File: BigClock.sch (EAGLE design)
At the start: 50 parts, among them IC12 LM317MBT, IC16 7805, IC5 74LS47N, IC6 74LS47N, IC7 74LS47N, IC8 74LS47N

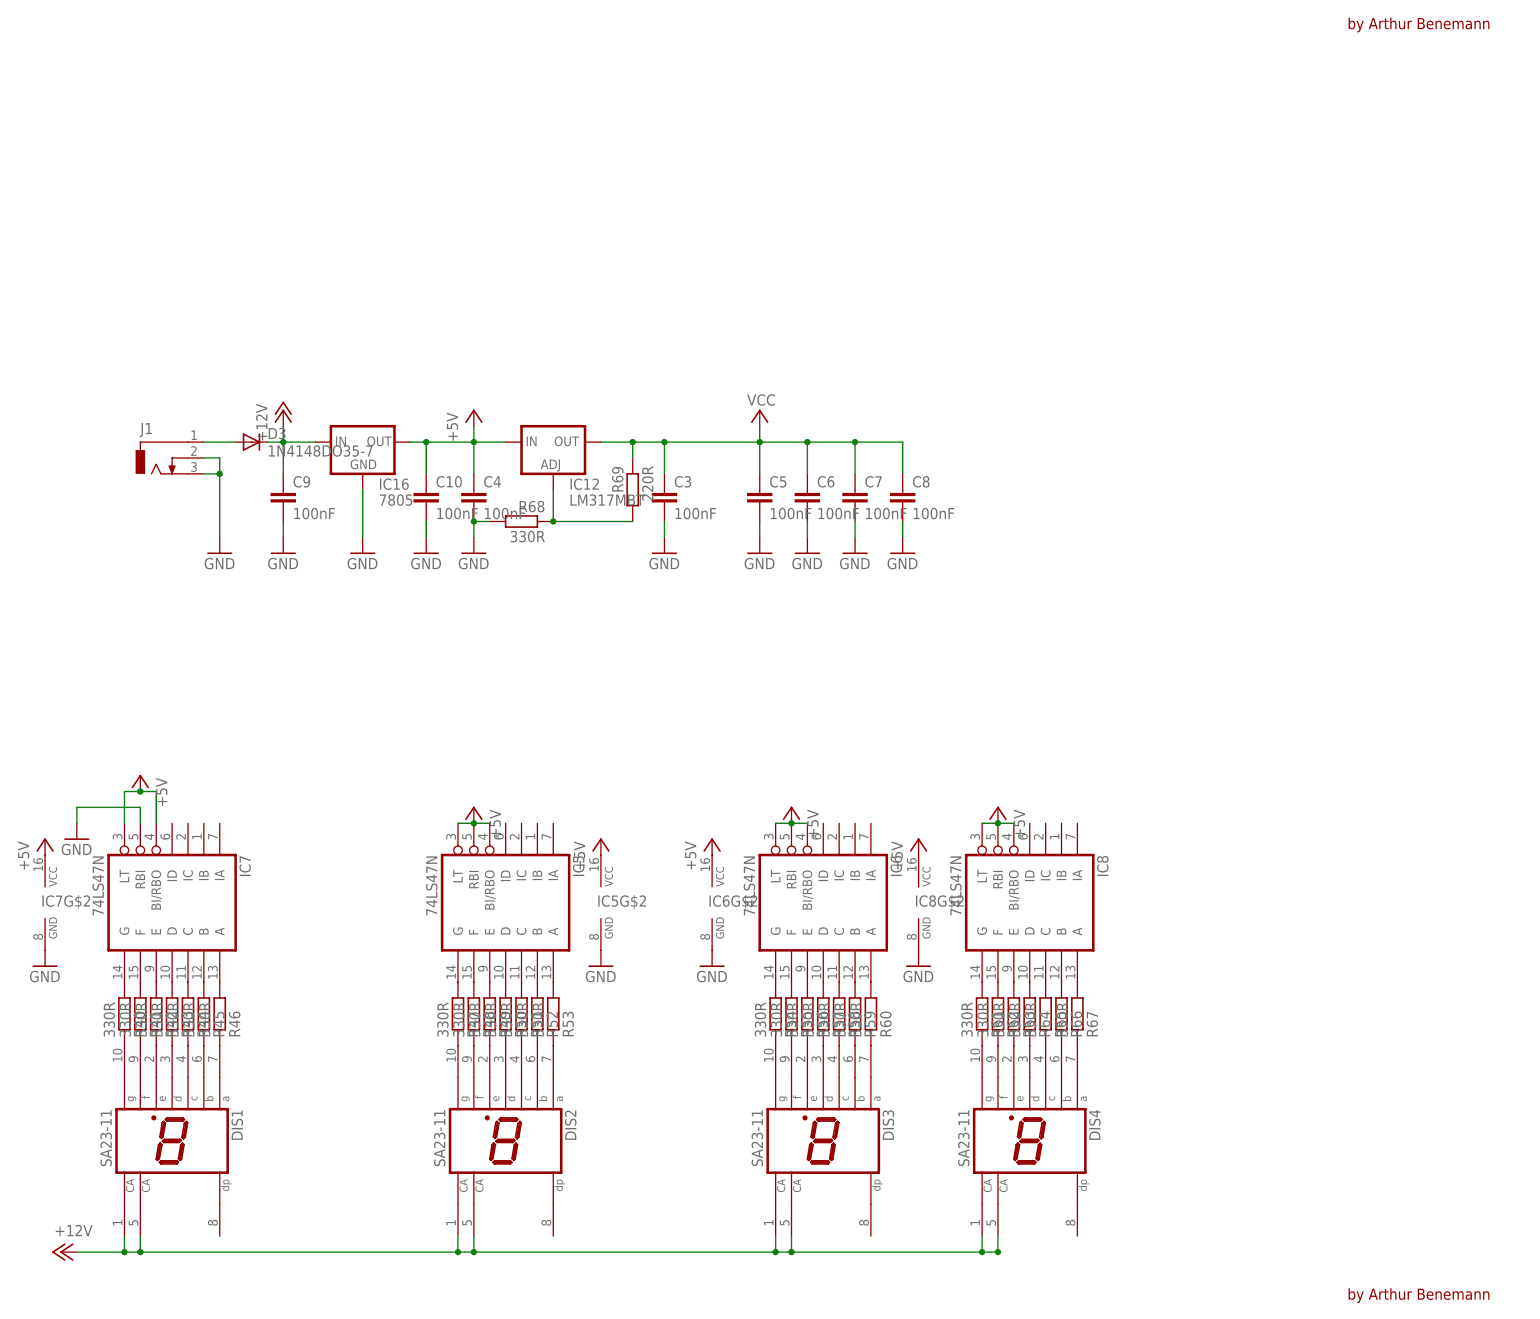
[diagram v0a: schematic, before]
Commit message: Displays routed on schematics
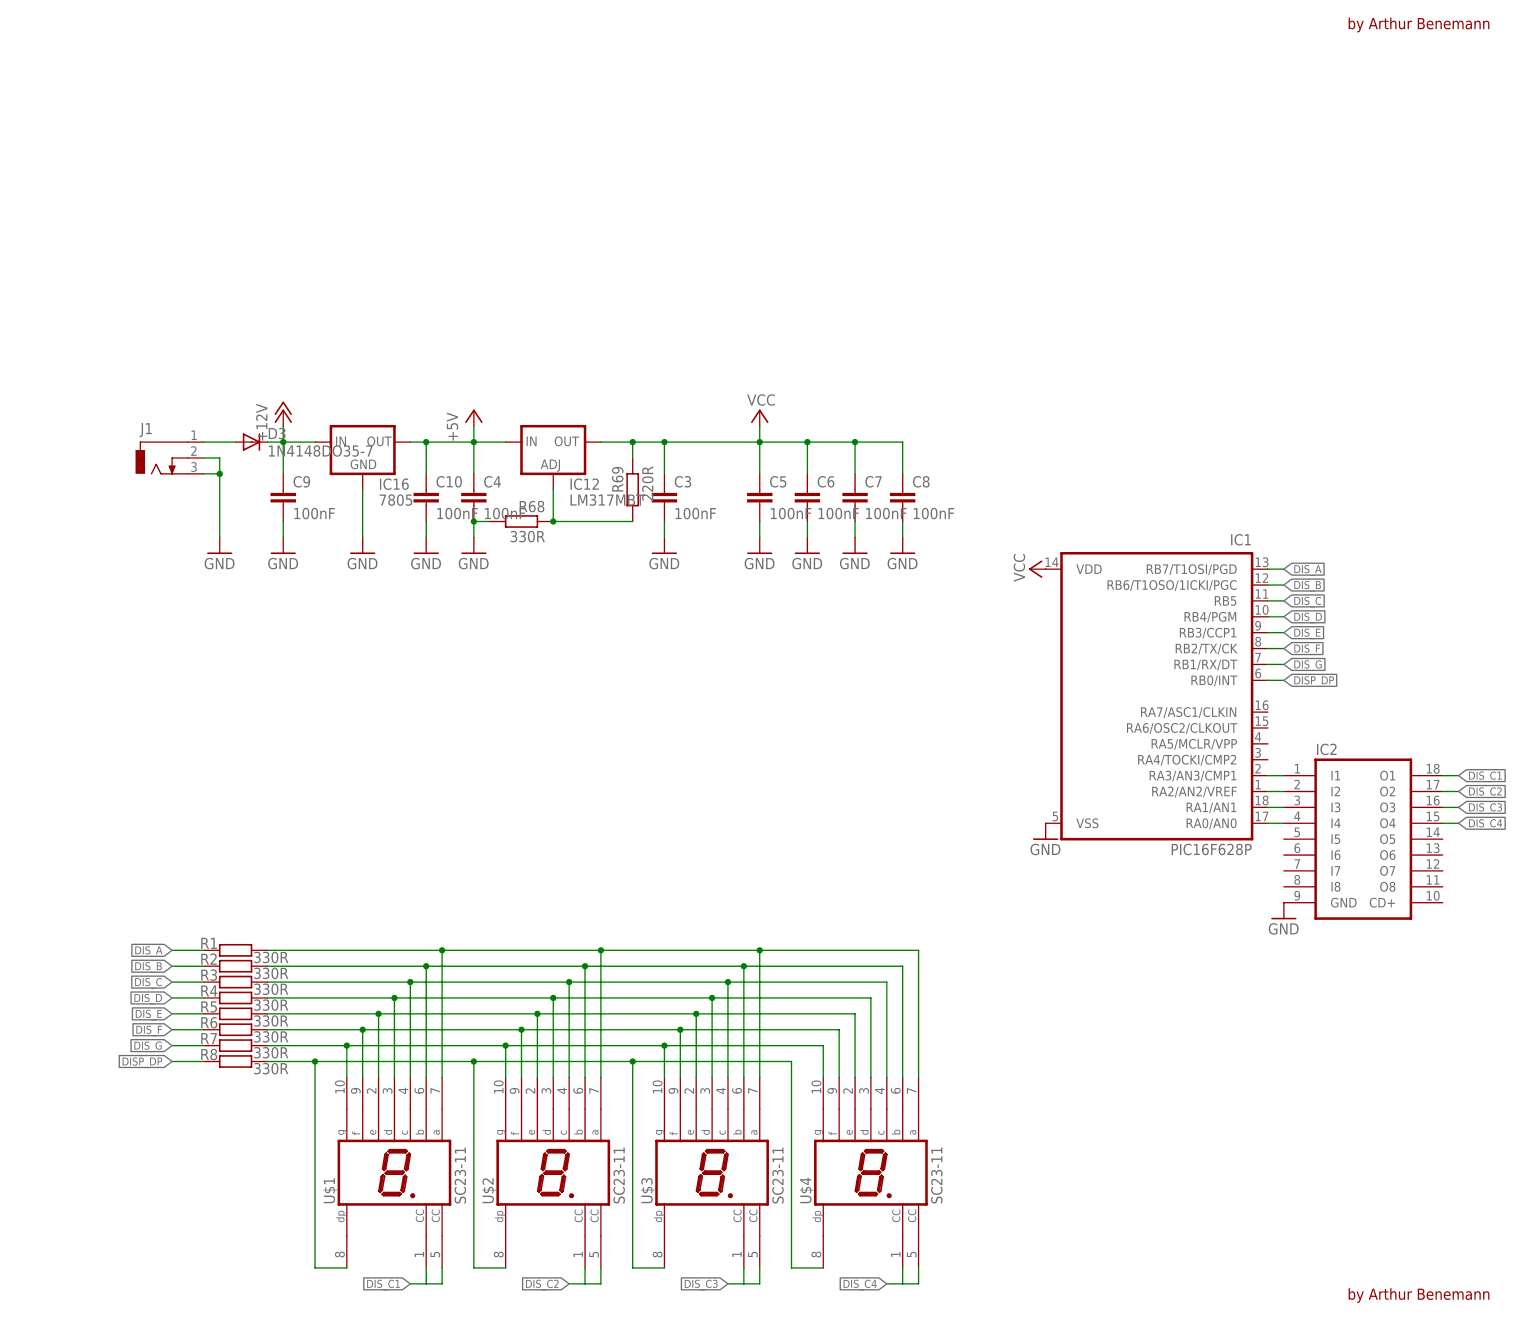
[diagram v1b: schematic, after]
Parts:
- removed DIS1, DIS2, DIS3, DIS4: SA23-11, display-kingbright:SA23-11
- removed IC5, IC6, IC7, IC8: 74LS47N, 74xx-eu:74LS47N
- removed R40, R41, R42, R43, R44, R45, R46, R47, R48, R49, R50, R51, R52, R53, R54, R55, R56, R57, R58, R59, R60, R61, R62, R63, R64, R65, R67: 330R, rcl:R-EU_0204/5
- removed R66: (no value), rcl:R-EU_0204/5
- added IC1: PIC16F628P, microchip:PIC16F628P
- added IC2: (no value), uln-udn:ULN2803A
- added R1, R2, R3, R4, R5, R6, R7, R8: 330R, rcl:R-EU_0204/5
- added U$1, U$2, U$3, U$4: SC23-11, display-kingbright:SC23-11
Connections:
- removed net N$10: DIS1.E, R42.1
- removed net N$100: IC6G$1.D, R57.2
- removed net N$101: IC6G$1.C, R58.2
- removed net N$102: IC6G$1.B, R59.2
- removed net N$103: IC6G$1.A, R60.2
- removed net N$104: DIS4.G, R61.1
- removed net N$105: DIS4.F, R62.1
- removed net N$106: DIS4.E, R63.1
- removed net N$107: DIS4.D, R64.1
- removed net N$108: DIS4.C, R65.1
- removed net N$109: DIS4.B, R66.1
- removed net N$11: IC7G$1.D, R43.2
- removed net N$110: DIS4.A, R67.1
- removed net N$111: IC8G$1.G, R61.2
- removed net N$112: IC8G$1.F, R62.2
- removed net N$113: IC8G$1.E, R63.2
- removed net N$114: IC8G$1.D, R64.2
- removed net N$115: IC8G$1.C, R65.2
- removed net N$116: IC8G$1.B, R66.2
- removed net N$117: IC8G$1.A, R67.2
- removed net N$24: DIS1.D, R43.1
- removed net N$25: IC7G$1.C, R44.2
- removed net N$26: DIS1.C, R44.1
- removed net N$27: IC7G$1.B, R45.2
- removed net N$28: DIS1.B, R45.1
- removed net N$29: IC7G$1.A, R46.2
- removed net N$30: DIS1.A, R46.1
- removed net N$38: IC5G$1.G, R47.2
- removed net N$39: IC5G$1.F, R48.2
- removed net N$40: IC5G$1.E, R49.2
- removed net N$41: IC5G$1.D, R50.2
- removed net N$42: IC5G$1.C, R51.2
- removed net N$43: IC5G$1.B, R52.2
- removed net N$44: IC5G$1.A, R53.2
- removed net N$6: DIS1.G, R40.1
- removed net N$7: IC7G$1.F, R41.2
- removed net N$8: DIS1.F, R41.1
- removed net N$88: DIS3.G, R54.1
- removed net N$9: IC7G$1.E, R42.2
- removed net N$91: DIS3.F, R55.1
- removed net N$92: DIS3.E, R56.1
- removed net N$93: DIS3.D, R57.1
- removed net N$94: DIS3.C, R58.1
- removed net N$95: DIS3.B, R59.1
- removed net N$96: DIS3.A, R60.1
- removed net N$97: IC6G$1.G, R54.2
- removed net N$98: IC6G$1.F, R55.2
- removed net N$99: IC6G$1.E, R56.2
- new net DISP_DP: IC1.RB0/INT, R8.2
- new net DIS_A: IC1.RB7/T1OSI/PGD, R1.2
- new net DIS_B: IC1.RB6/T1OSO/1ICKI/PGC, R2.2
- new net DIS_C: IC1.RB5, R3.2
- new net DIS_C1: IC2.O1, U$1.CC, U$1.CC@1
- new net DIS_C2: IC2.O2, U$2.CC, U$2.CC@1
- new net DIS_C3: IC2.O3, U$3.CC, U$3.CC@1
- new net DIS_C4: IC2.O4, U$4.CC, U$4.CC@1
- new net DIS_D: IC1.RB4/PGM, R4.2
- new net DIS_E: IC1.RB3/CCP1, R5.2
- new net DIS_F: IC1.RB2/TX/CK, R6.2
- new net DIS_G: IC1.RB1/RX/DT, R7.2
- new net N$1: R8.1, U$1.DP, U$2.DP, U$3.DP, U$4.DP
- new net N$2: IC1.RA3/AN3/CMP1, IC2.I1
- new net N$3: IC1.RA2/AN2/VREF, IC2.I2
- new net N$4: IC1.RA1/AN1, IC2.I3
- net +12V: no longer DIS1.CA, DIS1.CA@1, DIS2.CA, DIS2.CA@1, DIS3.CA, DIS3.CA@1, DIS4.CA, DIS4.CA@1
- net +5V: no longer IC5G$1.BI/RBO, IC5G$1.LT, IC5G$1.RBI, IC5G$2.VCC, IC6G$1.BI/RBO, IC6G$1.LT, IC6G$1.RBI, IC6G$2.VCC, IC7G$1.BI/RBO, IC7G$1.LT, IC7G$2.VCC, IC8G$1.BI/RBO, IC8G$1.LT, IC8G$1.RBI, IC8G$2.VCC
- net GND: now also IC1.VSS, IC2.GND; no longer IC5G$2.GND, IC6G$2.GND, IC7G$1.RBI, IC7G$2.GND, IC8G$2.GND
- net N$31: now also R7.1, U$1.G, U$2.G, U$3.G, U$4.G; no longer DIS2.G, R47.1
- net N$32: now also R6.1, U$1.F, U$2.F, U$3.F, U$4.F; no longer DIS2.F, R48.1
- net N$33: now also R5.1, U$1.E, U$2.E, U$3.E, U$4.E; no longer DIS2.E, R49.1
- net N$34: now also R4.1, U$1.D, U$2.D, U$3.D, U$4.D; no longer DIS2.D, R50.1
- net N$35: now also R3.1, U$1.C, U$2.C, U$3.C, U$4.C; no longer DIS2.C, R51.1
- net N$36: now also R2.1, U$1.B, U$2.B, U$3.B, U$4.B; no longer DIS2.B, R52.1
- net N$37: now also R1.1, U$1.A, U$2.A, U$3.A, U$4.A; no longer DIS2.A, R53.1
- net N$5: now also IC1.RA0/AN0, IC2.I4; no longer IC7G$1.G, R40.2
- net VCC: now also IC1.VDD
